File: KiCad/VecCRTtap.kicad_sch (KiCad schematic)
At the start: 30 parts, among them J1 Conn_02x08_Top_Bottom, J2 Conn_02x08_Top_Bottom, J3 X, J4 Y, J5 Z, K1 KLINKE_3POL, K2 1UM, Q1 BS250, Q2 BS170

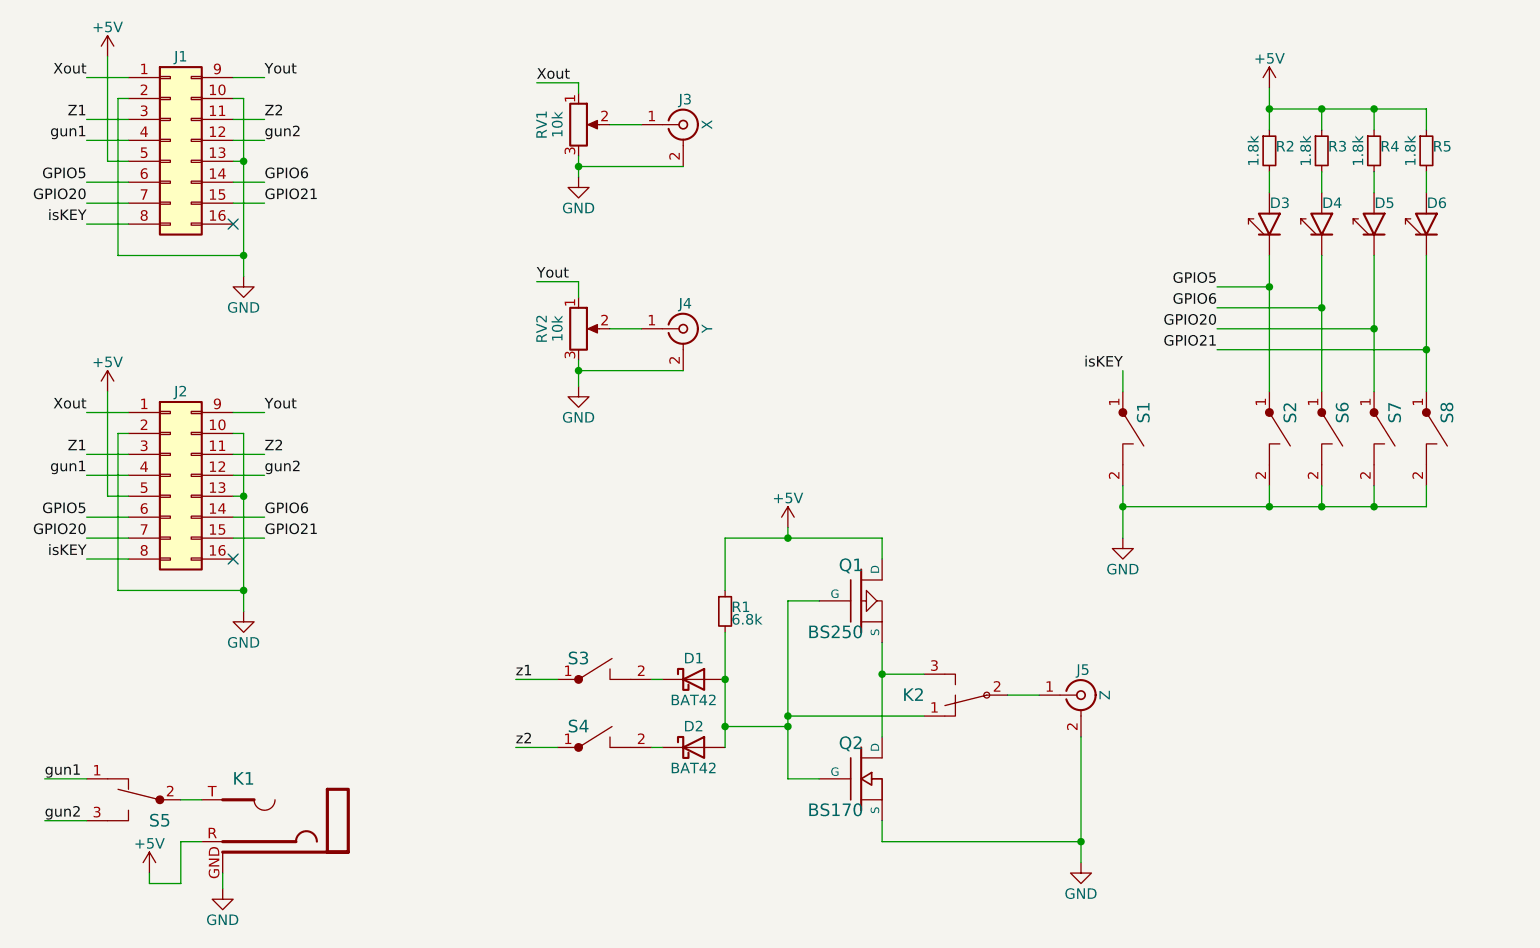
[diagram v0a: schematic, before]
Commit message: KiCad: EDA updates for PCB production; preliminary tap and switches; ReadMe.md updated
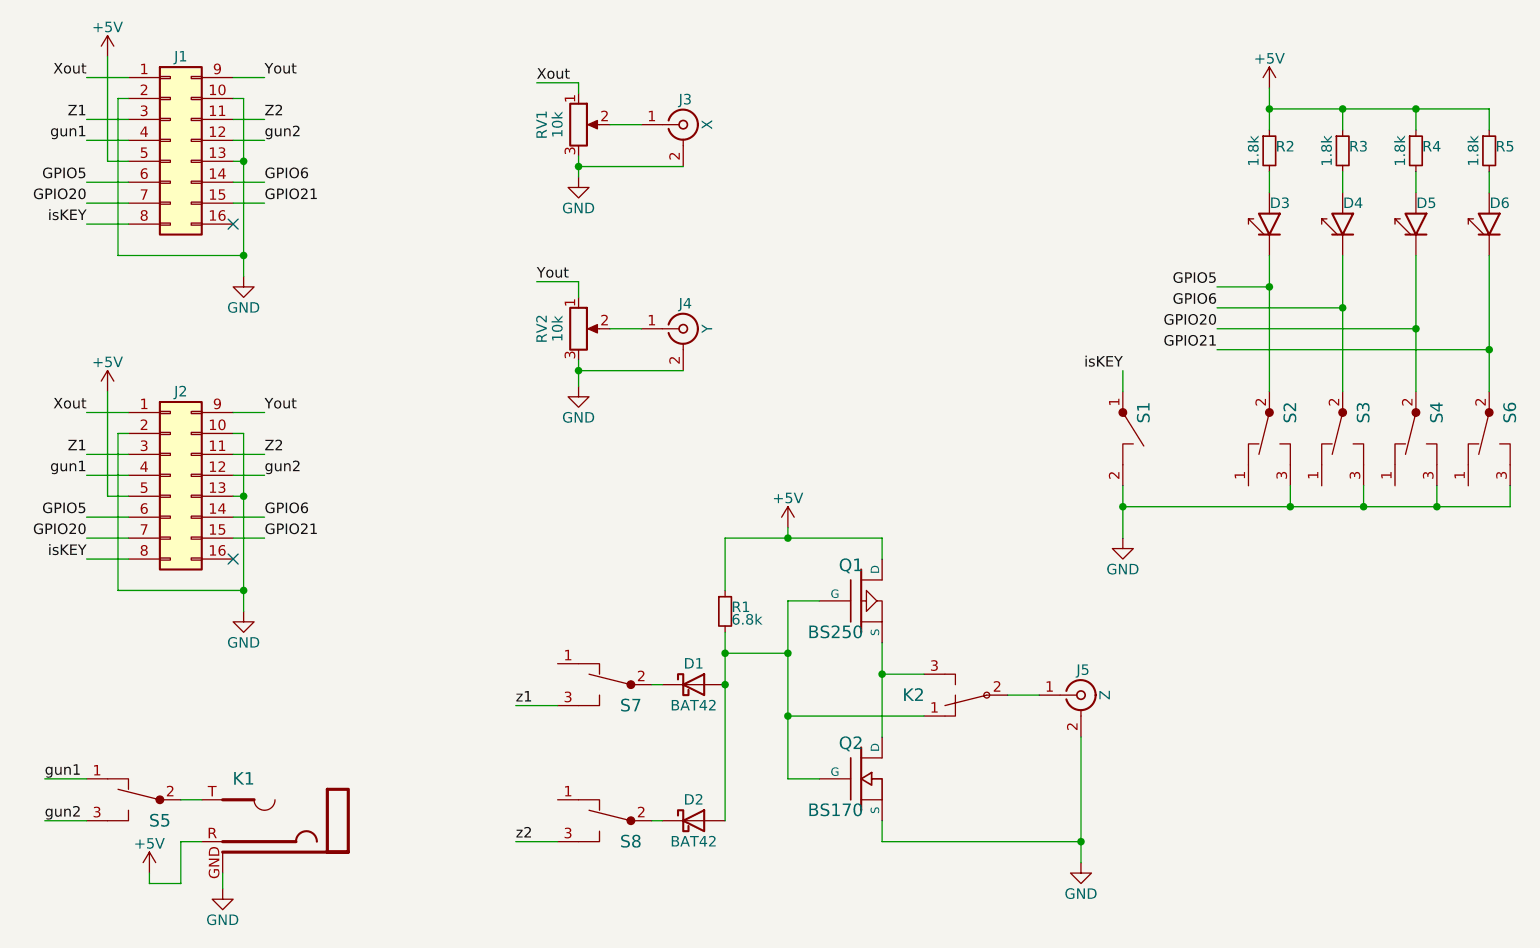
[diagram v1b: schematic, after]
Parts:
- removed S2, S3, S4, S6, S7, S8: TASTER, symbol rg:TASTER
- added S2, S3, S4, S6, S7, S8: TASTERU, RG:Sw-T101-Um, symbol rg:TASTERU
- D3, D4, D5, D6: footprint (none) -> RG:LED_D5.0mm
- J1, J2: footprint (none) -> RG:Wannenstecker_2x08_V
- J3, J4, J5: footprint (none) -> Connector_Coaxial:SMB_Jack_Vertical
- K1: footprint LumbergKlinke3,5mm -> RG:LumbergKlinke3,5mm
- K2: footprint PIN_ARRAY_3x1 -> RG:Pins_3
- R1, R2, R3, R4, R5: footprint (none) -> RG:R4-2
- RV1, RV2: footprint (none) -> RG:ACP-CA9V10-Trimmer
- S1: footprint (none) -> RG:Tast2mil
- S5: footprint (none) -> RG:Sw-T101-Um
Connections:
- net GND: now also S2.3, S3.3, S4.3, S6.3
- net GPIO20: now also S4.2
- net GPIO21: now also S6.2
- net GPIO5: now also S2.2
- net GPIO6: now also S3.2
- net z1: now also S7.3
- net z2: now also S8.3
- net at D1.1 (K): now also S7.2
- net at D2.1 (K): now also S8.2
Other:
- moved on the sheet: D1, D2, D4, D5, D6, R3, R4, R5

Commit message: revise tap board
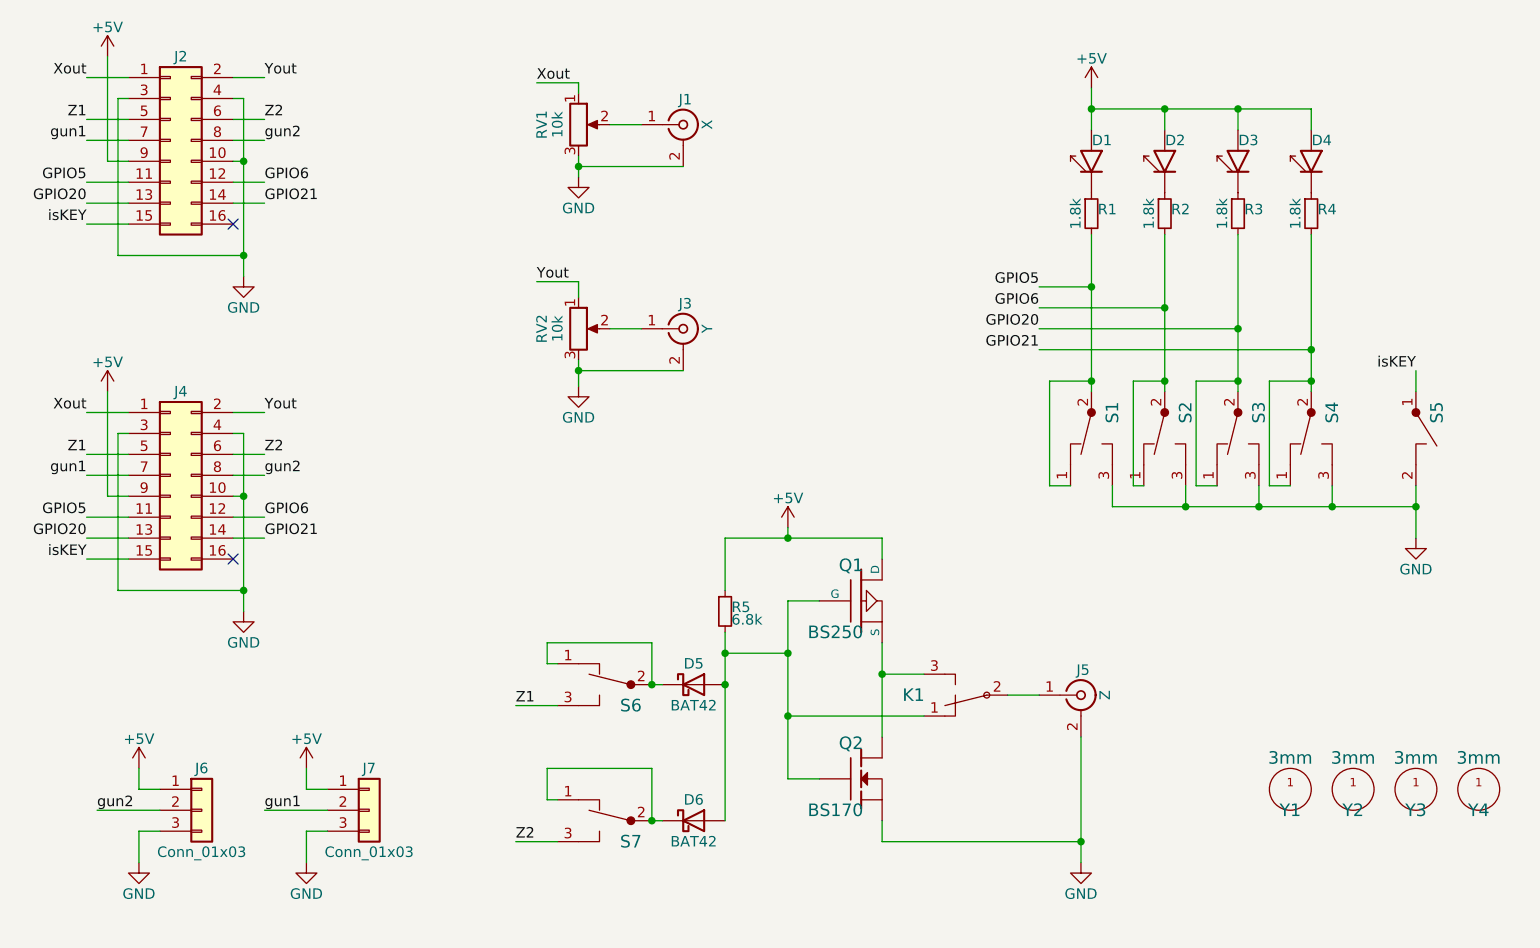
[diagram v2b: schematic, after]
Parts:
- removed D5, D6: LED, RG:LED_D5.0mm, symbol rg:LED
- removed J1, J2: Conn_02x08_Top_Bottom, RG:Wannenstecker_2x08_V, symbol Connector_Generic:Conn_02x08_Top_Bottom
- removed K1: KLINKE_3POL, RG:LumbergKlinke3,5mm, symbol rg:KLINKE_3POL
- removed S5: TASTERU, RG:Sw-T101-Um, symbol rg:TASTERU
- added D1, D2: LED, RG:LED_D5.0mm, symbol rg:LED
- added J2, J4: Conn_02x08_Odd_Even, RG:Wannenstecker_2x08_V, symbol Connector_Generic:Conn_02x08_Odd_Even
- added J6, J7: Conn_01x03, RG:PSS_3, symbol Connector_Generic:Conn_01x03
- added Y1, Y2, Y3, Y4: 3mm, RG:Bohrloch3mm, symbol rg:BOHRLOCH
- D5: renamed from D1; footprint Diode_THT:D_DO-35_SOD27_P7.62mm_Horizontal -> RG:D3
- D6: renamed from D2; footprint Diode_THT:D_DO-35_SOD27_P7.62mm_Horizontal -> RG:D3
- J1: renamed from J3; footprint Connector_Coaxial:SMB_Jack_Vertical -> RG:Cinch_liegend
- J3: renamed from J4; footprint Connector_Coaxial:SMB_Jack_Vertical -> RG:Cinch_liegend
- J5: footprint Connector_Coaxial:SMB_Jack_Vertical -> RG:Cinch_liegend
- renumbered K2 to K1, R2 to R1, R3 to R2, R4 to R3, R5 to R4, R1 to R5, S2 to S1, S3 to S2, S4 to S3, S6 to S4, S1 to S5, S7 to S6, S8 to S7
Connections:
- net z1 is gone; now on net Z1: S6.3
- net z2 is gone; now on net Z2: S7.3
- net +5V: now also D3.A, D4.A, D1.A, D2.A, J2.9 (Pin_9), J4.9 (Pin_9), J6.1 (Pin_1), J7.1 (Pin_1); no longer R1.1, R2.1, R3.1, R4.1
- net GND: now also J2.10 (Pin_10), J2.3 (Pin_3), J2.4 (Pin_4), J4.10 (Pin_10), J4.3 (Pin_3), J4.4 (Pin_4), J6.3 (Pin_3), J7.3 (Pin_3)
- net GPIO20: now also R3.2, S3.1, J2.13 (Pin_13), J4.13 (Pin_13)
- net GPIO21: now also R4.2, S4.1, J2.14 (Pin_14), J4.14 (Pin_14)
- net GPIO5: now also R1.2, S1.1, J2.11 (Pin_11), J4.11 (Pin_11); no longer D3.K
- net GPIO6: now also R2.2, S2.1, J2.12 (Pin_12), J4.12 (Pin_12); no longer D4.K
- net Xout: now also J2.1 (Pin_1), J4.1 (Pin_1)
- net Yout: now also J2.2 (Pin_2), J4.2 (Pin_2)
- net Z1: now also J2.5 (Pin_5), J4.5 (Pin_5)
- net Z2: now also J2.6 (Pin_6), J4.6 (Pin_6)
- net gun1: now also J2.7 (Pin_7), J4.7 (Pin_7), J7.2 (Pin_2)
- net gun2: now also J2.8 (Pin_8), J4.8 (Pin_8), J6.2 (Pin_2)
- net isKEY: now also J2.15 (Pin_15), J4.15 (Pin_15)
- net at S6.1: now also D5.1 (K), S6.2
- net at S7.1: now also D6.1 (K), S7.2
- new net: D3.K, R3.1
- new net: D1.K, R1.1
- new net: D2.K, R2.1
- new net: D4.K, R4.1
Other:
- moved on the sheet: R1, R2, R3, R4, S1, S2, S3, S4, S5
